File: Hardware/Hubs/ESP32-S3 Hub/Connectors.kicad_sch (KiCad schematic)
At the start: 23 parts, among them J1 Precidip 853-87-004-20-001101, J10 Precidip 853-87-004-20-001101, J11 7 pin FPC 0.3mm Aces 51688-00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, J12 Precidip 853-87-004-20-001101, J13 TE 3-2363961-0 receptacle, J15 Precidip 853-87-004-20-001101, J16 TE 3-2363961-0 receptacle, J18 Precidip 852-10-004-20-001101, J2 Precidip 853-87-004-20-001101, J3 7 pin FPC 0.3mm Aces 51688-00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, J4 Precidip 853-87-004-20-001101, J5 7 pin FPC 0.3mm Aces 51688-00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, J6 Precidip 853-87-004-20-001101, J7 Precidip 853-87-004-20-001101, J8 7 pin FPC 0.3mm Aces 51688-00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, J9 Precidip 853-87-004-20-001101

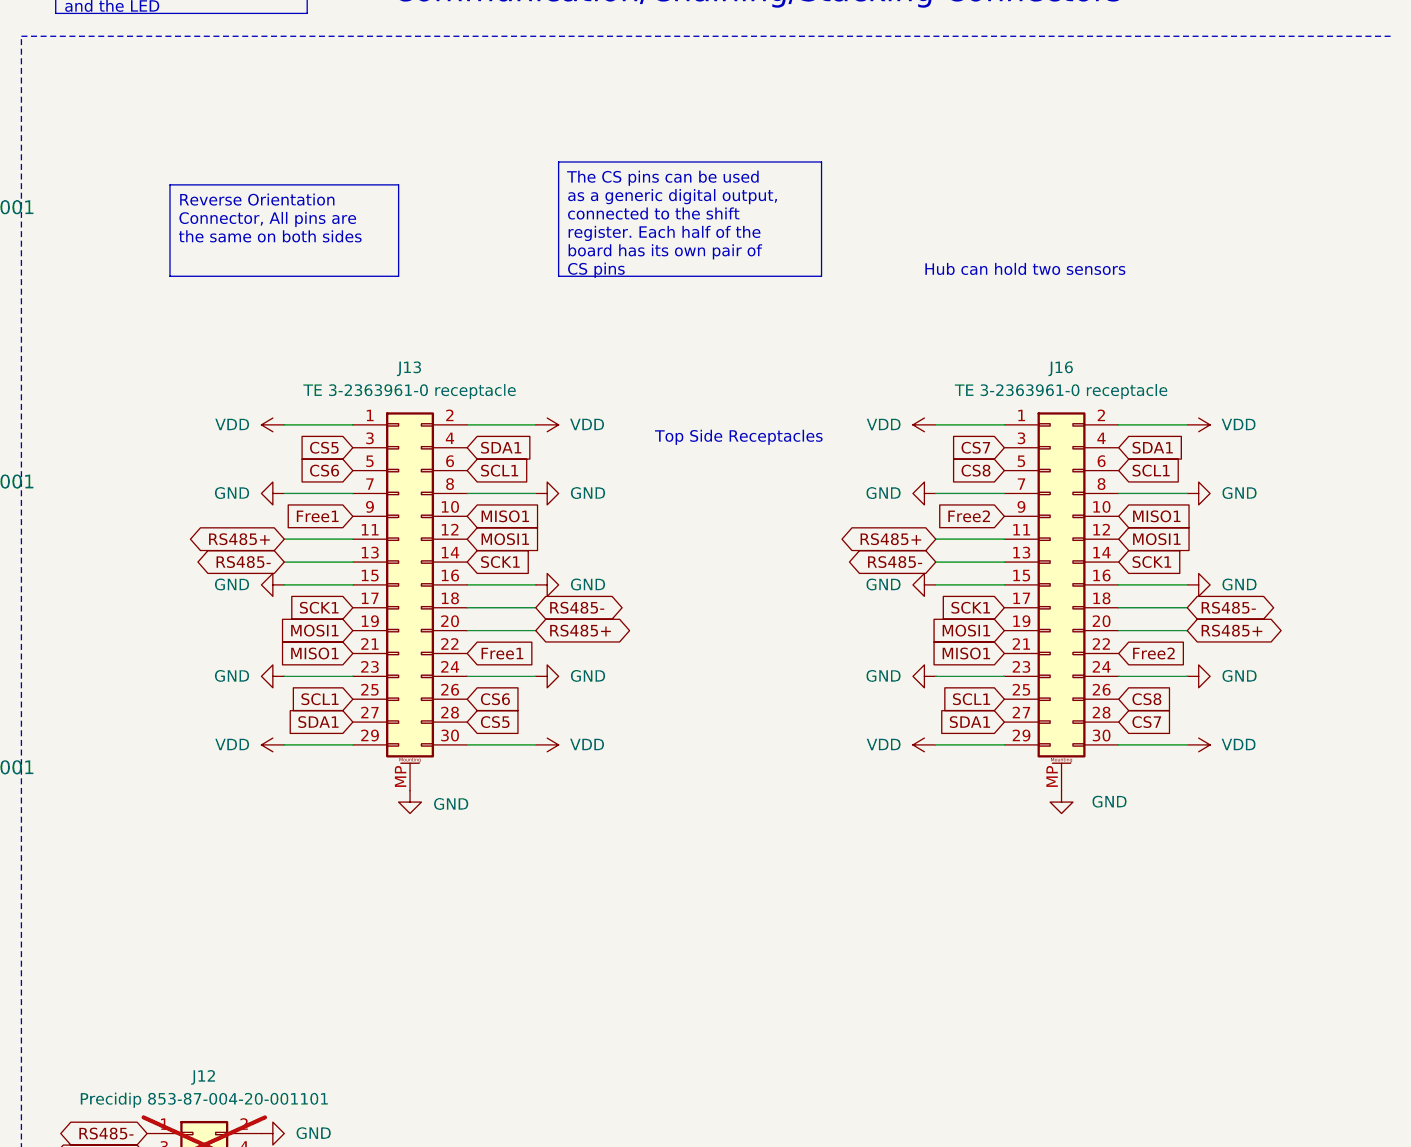
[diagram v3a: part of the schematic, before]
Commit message: Changed peripheral, tied PWM to shift reg, program pins
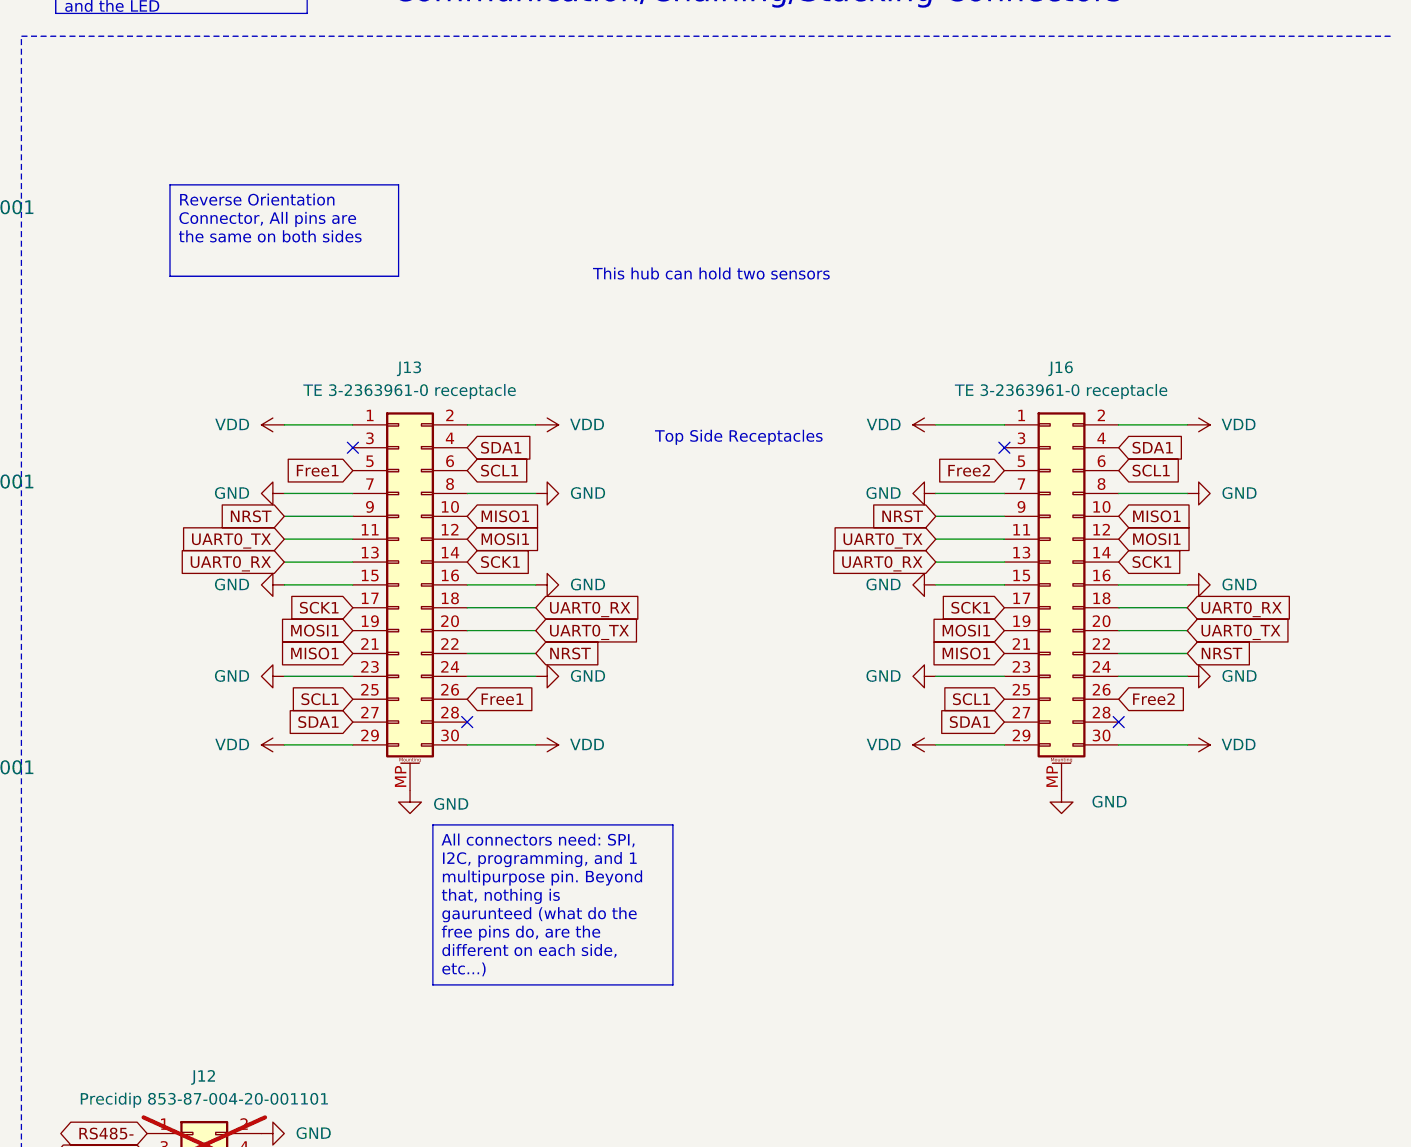
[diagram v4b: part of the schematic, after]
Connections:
- net CS6 is gone; now on net Free1: J13.26 (Pin_26), J13.5 (Pin_5)
- net CS8 is gone; now on net Free2: J16.26 (Pin_26), J16.5 (Pin_5)
- net Free1: no longer J13.22 (Pin_22), J13.9 (Pin_9)
- net Free2: no longer J16.22 (Pin_22), J16.9 (Pin_9)
- net RS485+: no longer J13.11 (Pin_11), J13.20 (Pin_20), J16.11 (Pin_11), J16.20 (Pin_20)
- net RS485-: no longer J13.13 (Pin_13), J13.18 (Pin_18), J16.13 (Pin_13), J16.18 (Pin_18)
- net UART0_RX: now also J13.13 (Pin_13), J13.18 (Pin_18), J16.13 (Pin_13), J16.18 (Pin_18)
- net UART0_TX: now also J13.11 (Pin_11), J13.20 (Pin_20), J16.11 (Pin_11), J16.20 (Pin_20)
- net CS5: no longer names the net of J13.28 (Pin_28)
- net CS5: no longer J13.3 (Pin_3)
- net CS7: no longer names the net of J16.28 (Pin_28)
- net CS7: no longer J16.3 (Pin_3)
- new net NRST: J13.22 (Pin_22), J13.9 (Pin_9), J16.22 (Pin_22), J16.9 (Pin_9)
- no-connect marks 3 -> 7
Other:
- note added: "This hub can hold two sensors"
- note removed: "Hub can hold two sensors"

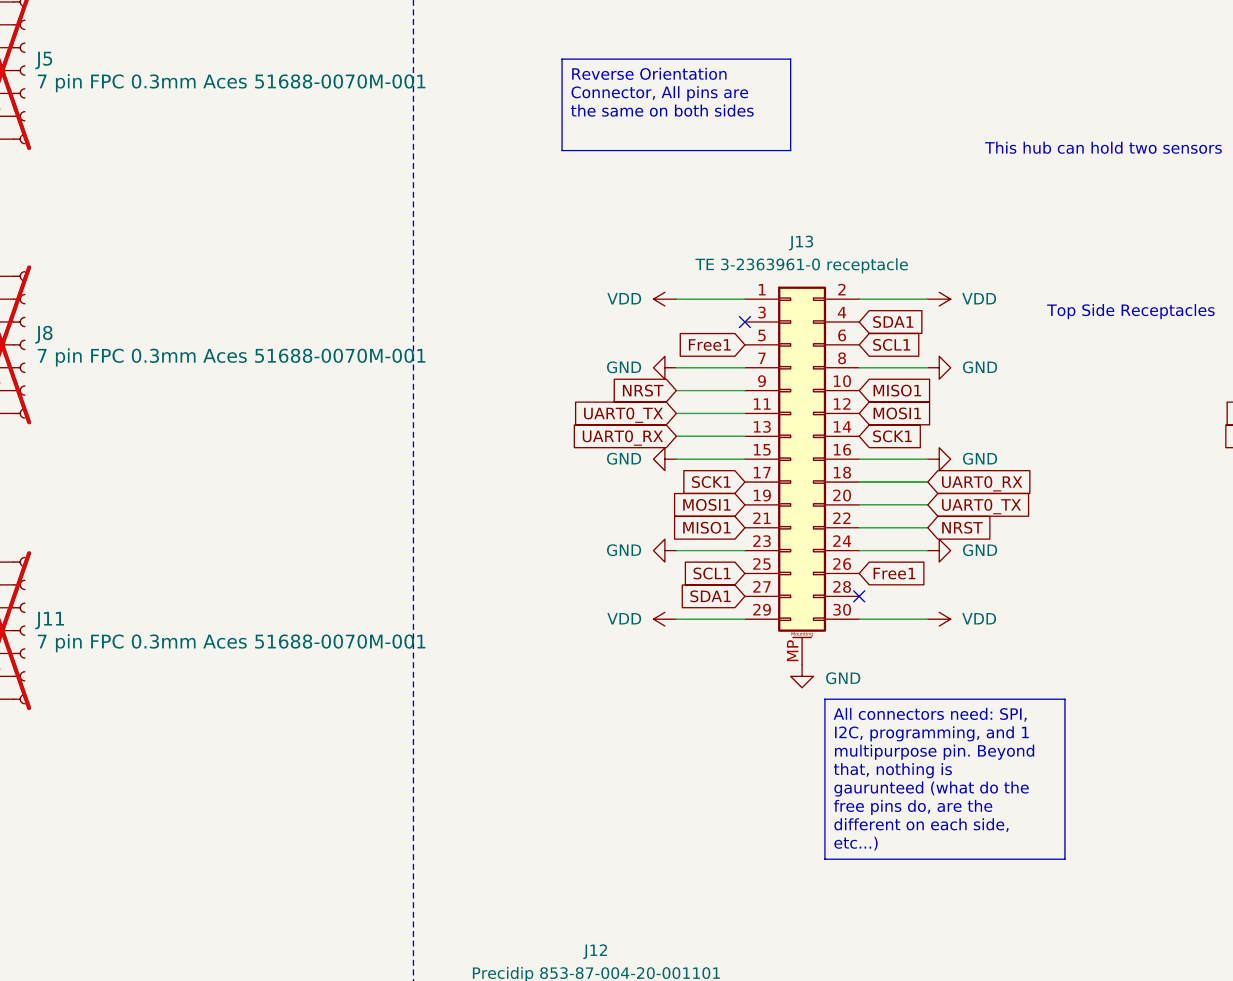
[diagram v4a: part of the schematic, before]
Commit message: Added future design expansion comments, re arrange components to fit better
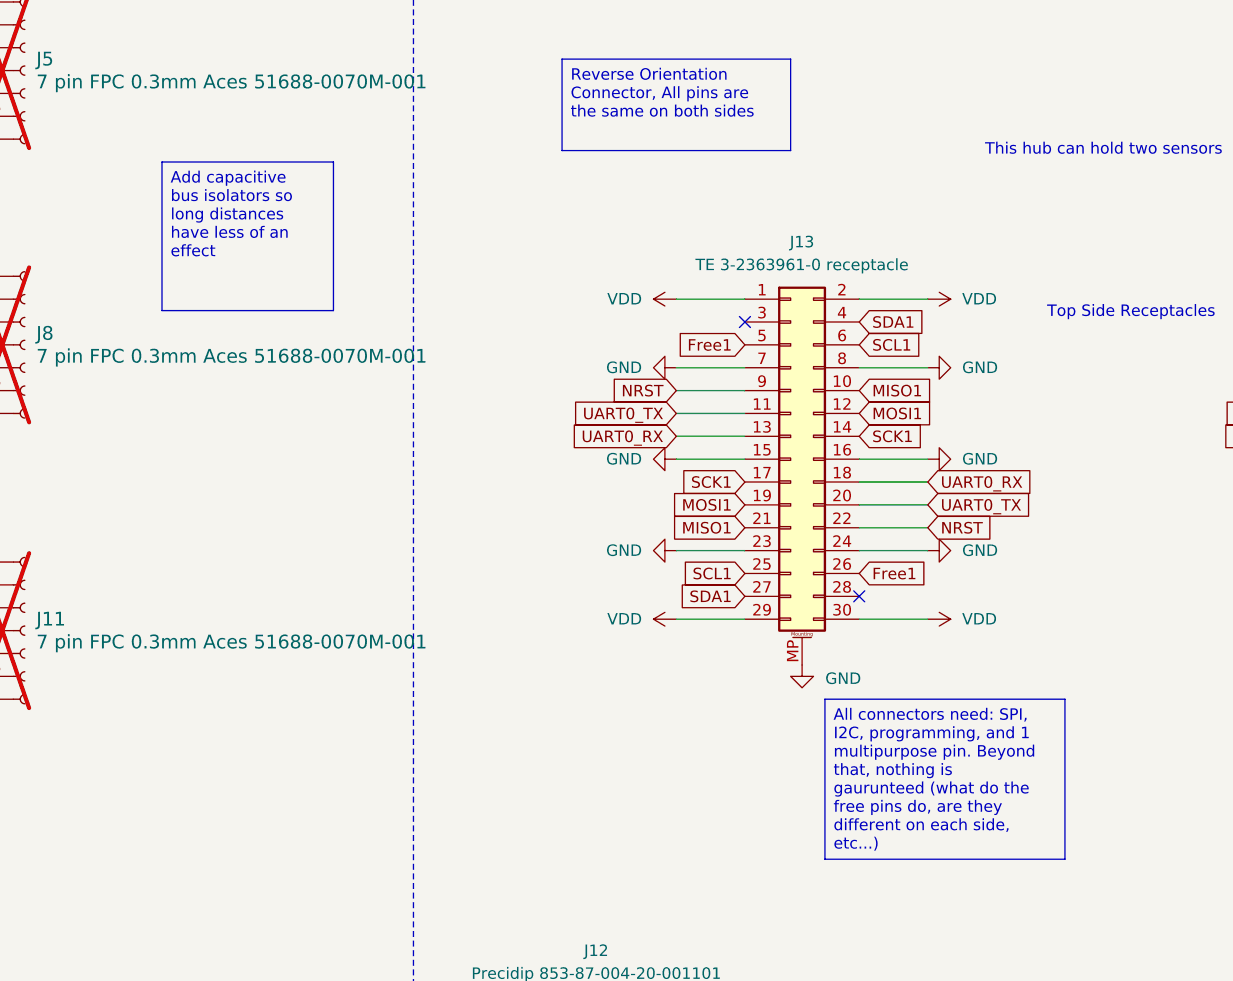
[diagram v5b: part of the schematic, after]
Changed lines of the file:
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@@
+		)
+	)
+	(text_box "Add capacitive bus isolators so long distances have less of an effect"
+		(exclude_from_sim no)
+		(at 105.41 80.01 0)
+		(size 19.05 16.51)
+		(margins 0.9525 0.9525 0.9525 0.9525)
+		(stroke
+			(width 0)
+			(type solid)
+		)
+		(fill
+			(type none)
+		)
+		(effects
+			(font
+				(size 1.27 1.27)
+			)
+			(justify left top)
 		)
 	)
@@
 		)
 	)
-	(text_box "All connectors need: SPI, I2C, programming, and 1 multipurpose pin. Beyond that, nothing is gaurunteed (what do the free pins do, are the different on each side, etc...)\n"
+	(text_box "All connectors need: SPI, I2C, programming, and 1 multipurpose pin. Beyond that, nothing is gaurunteed (what do the free pins do, are they different on each side, etc...)\n"
 		(exclude_from_sim no)
 		(at 179.07 139.7 0)
